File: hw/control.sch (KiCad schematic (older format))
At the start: 12 parts, among them U201 XTAL_OSC, U202 74HC74, U203 74HC161, U204 74HC574, U205 27C64, U206 27C64, U207 27C64, U208 27C64, U209 74HCT574, U210 74HCT574, U211 74HCT574, U212 74HCT574

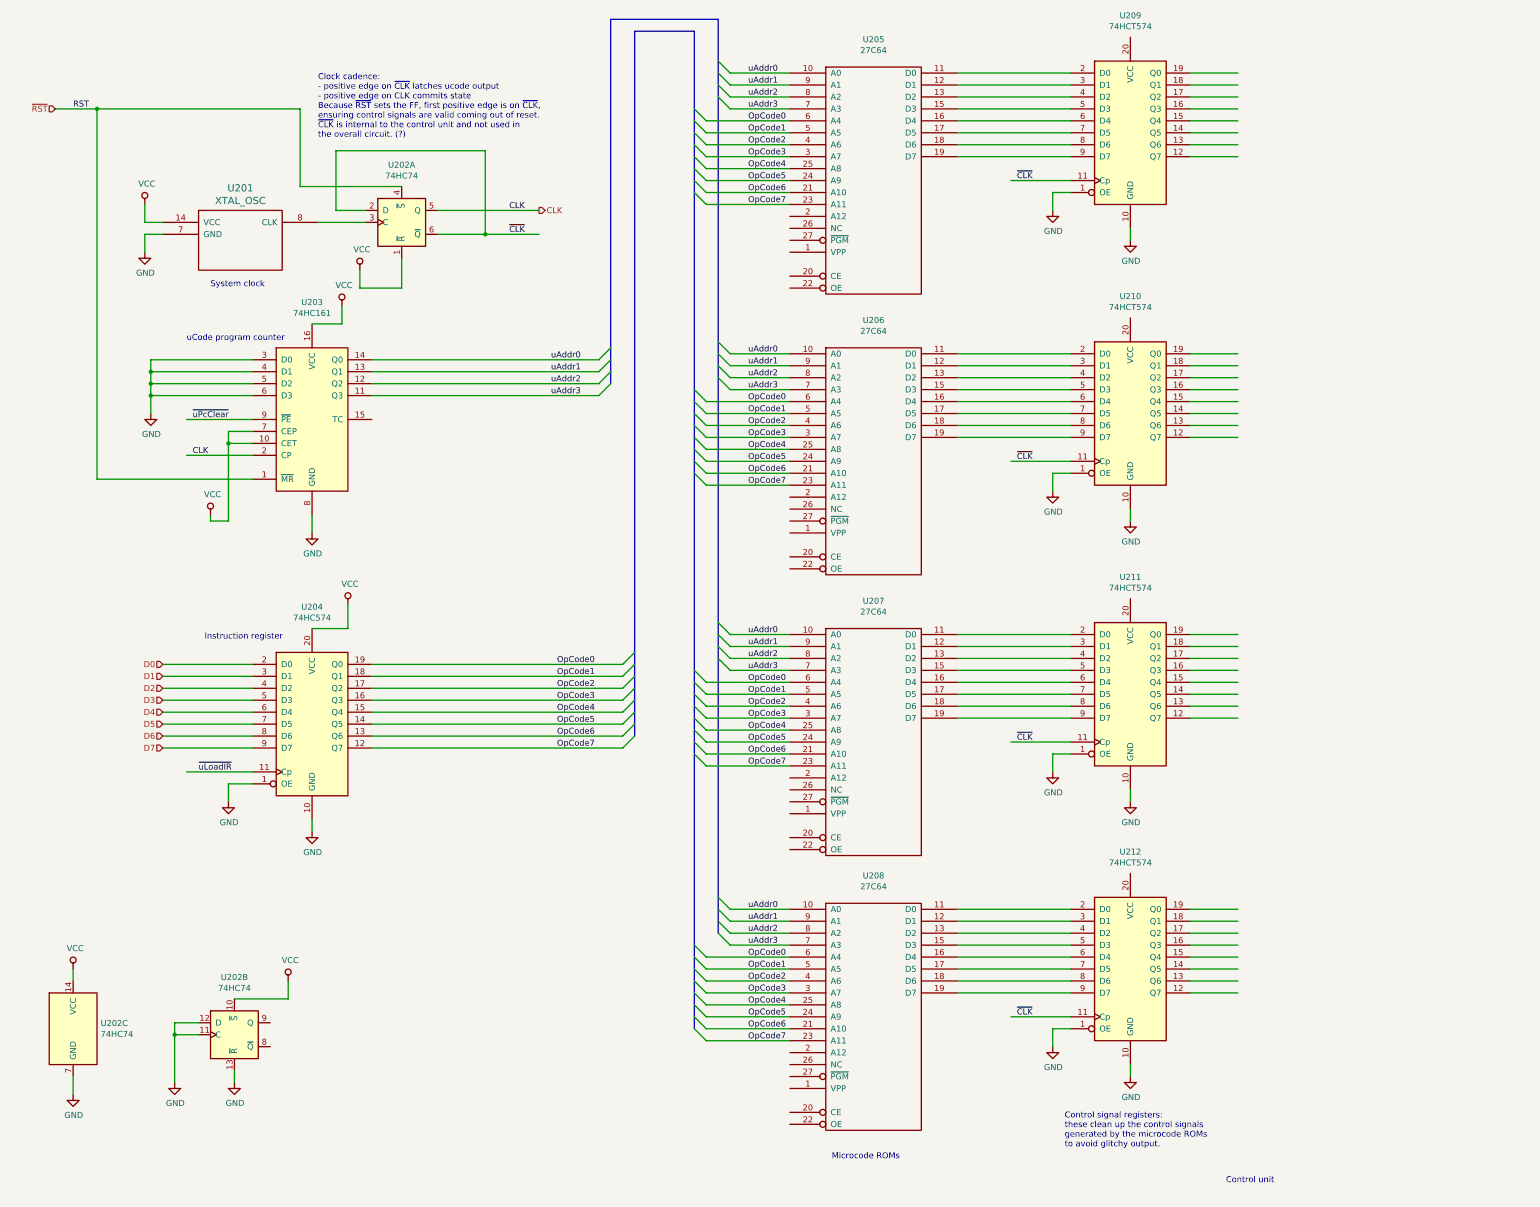
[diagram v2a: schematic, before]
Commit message: control cleanup, generate proper clock for IR load
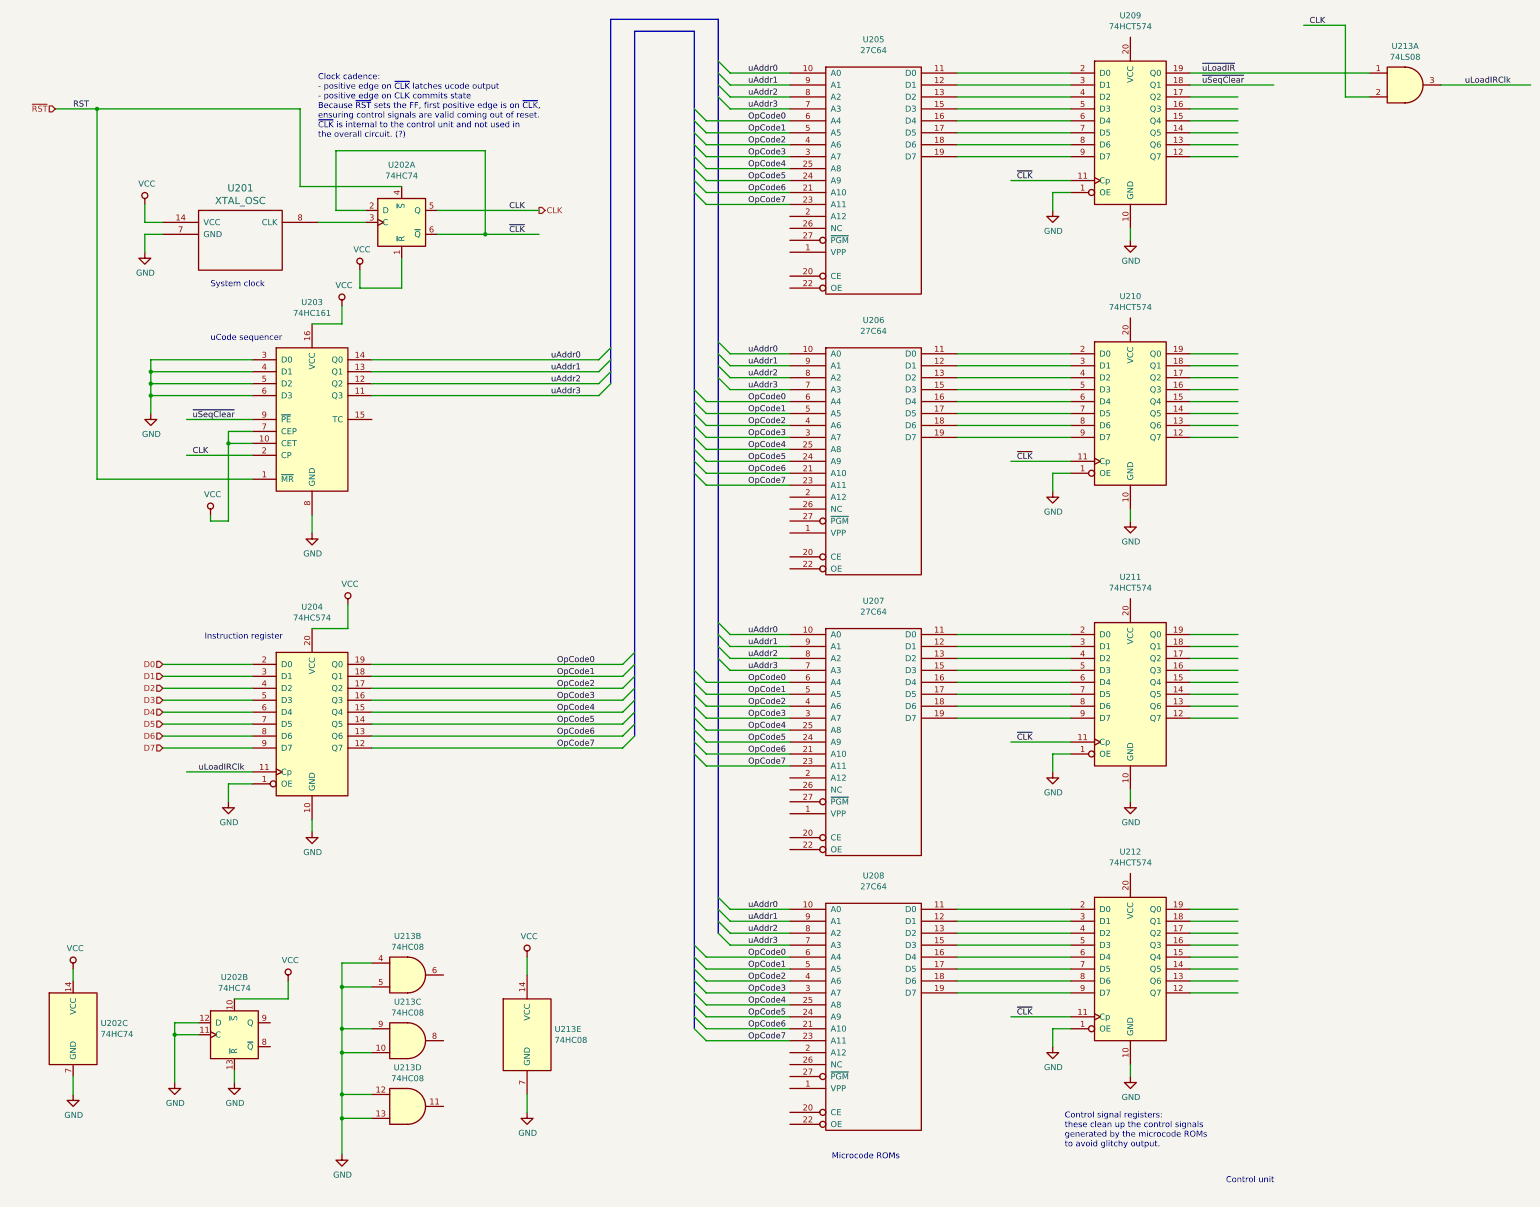
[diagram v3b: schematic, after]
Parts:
- added U213: 74LS08, symbol 74xx:74LS08
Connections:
- net labels added: uLoadIRClk, ~uSeqClear
- net labels removed: ~uPcClear
- wire segments 203 -> 221
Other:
- note added: "uCode sequencer"
- note removed: "uCode program counter"
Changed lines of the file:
@@
 	2650 3950 2100 3950
 Text Label 2150 3950 0    50   ~ 0
-~uPcClear
+~uSeqClear
 Wire Wire Line
 	2650 4250 2100 4250
@@
 	1    0    0    -1
 $EndComp
-Text Notes 2100 3300 0    50   ~ 0
-uCode program counter
+Text Notes 2300 3300 0    50   ~ 0
+uCode sequencer
 Text Label 5150 3450 0    50   ~ 0
 uAddr0
@@
 OpCode7
 Text Label 2200 6900 0    50   ~ 0
-~uLoadIR
+uLoadIRClk
 Wire Wire Line
 	3650 3450 5550 3450
@@
 $EndComp
 Wire Wire Line
-	10500 1050 10900 1050
-Wire Wire Line
-	10500 1150 10900 1150
-Wire Wire Line
 	10500 1250 10900 1250
 Wire Wire Line
@@
 Text Notes 9450 10050 0    50   ~ 0
 Control signal registers:\nthese clean up the control signals\ngenerated by the microcode ROMs\nto avoid glitchy output.
+$Comp
+L 74xx:74LS08 U213
+U 1 1 5DA375ED
+P 12300 1150
+F 0 "U213" H 12300 1475 50  0000 C CNN
+F 1 "74LS08" H 12300 1384 50  0000 C CNN
+F 2 "" H 12300 1150 50  0001 C CNN
+F 3 "" H 12300 1150 50  0001 C CNN
+	1    12300 1150
+	1    0    0    -1
+$EndComp
+Wire Wire Line
+	12000 1250 11800 1250
+Wire Wire Line
+	11800 1250 11800 650
+Wire Wire Line
+	11800 650  11450 650
+Text Label 11500 650  0    50   ~ 0
+CLK
+Wire Wire Line
+	10500 1050 12000 1050
+Text Label 10600 1050 0    50   ~ 0
+~uLoadIR
+Wire Wire Line
+	12600 1150 13350 1150
+Text Label 12800 1150 0    50   ~ 0
+uLoadIRClk
+Wire Wire Line
+	10500 1150 11200 1150
+Text Label 10600 1150 0    50   ~ 0
+~uSeqClear
+$Comp
+L 74xx:74LS08 U213
+U 2 1 5DA7CE65
+P 3950 8600
+F 0 "U213" H 3950 8925 50  0000 C CNN
+F 1 "74HC08" H 3950 8834 50  0000 C CNN
+F 2 "" H 3950 8600 50  0001 C CNN
+F 3 "" H 3950 8600 50  0001 C CNN
+	2    3950 8600
+	1    0    0    -1
+$EndComp
+$Comp
+L 74xx:74LS08 U213
+U 3 1 5DA7E038
+P 3950 9150
+F 0 "U213" H 3950 9475 50  0000 C CNN
+F 1 "74HC08" H 3950 9384 50  0000 C CNN
+F 2 "" H 3950 9150 50  0001 C CNN
+F 3 "" H 3950 9150 50  0001 C CNN
+	3    3950 9150
+	1    0    0    -1
+$EndComp
+$Comp
+L 74xx:74LS08 U213
+U 4 1 5DA82038
+P 3950 9700
+F 0 "U213" H 3950 10025 50  0000 C CNN
+F 1 "74HC08" H 3950 9934 50  0000 C CNN
+F 2 "" H 3950 9700 50  0001 C CNN
+F 3 "" H 3950 9700 50  0001 C CNN
+	4    3950 9700
+	1    0    0    -1
+$EndComp
+Wire Wire Line
+	3650 8500 3400 8500
+Wire Wire Line
+	3400 8500 3400 8700
+Wire Wire Line
+	3650 8700 3400 8700
+Connection ~ 3400 8700
+Wire Wire Line
+	3400 8700 3400 9050
+Wire Wire Line
+	3650 9050 3400 9050
+Connection ~ 3400 9050
+Wire Wire Line
+	3400 9050 3400 9250
+Wire Wire Line
+	3650 9250 3400 9250
+Connection ~ 3400 9250
+Wire Wire Line
+	3400 9250 3400 9600
+Wire Wire Line
+	3650 9600 3400 9600
+Connection ~ 3400 9600
+Wire Wire Line
+	3400 9600 3400 9800
+Wire Wire Line
+	3650 9800 3400 9800
+Connection ~ 3400 9800
+Wire Wire Line
+	3400 9800 3400 10100
+$Comp
+L 74xx:74LS08 U213
+U 5 1 5DAFA716
+P 4950 9100
+F 0 "U213" H 5180 9146 50  0000 L CNN
+F 1 "74HC08" H 5180 9055 50  0000 L CNN
+F 2 "" H 4950 9100 50  0001 C CNN
+F 3 "" H 4950 9100 50  0001 C CNN
+	5    4950 9100
+	1    0    0    -1
+$EndComp
+$Comp
+L power:GND #PWR?
+U 1 1 5DAFC25E
+P 3400 10100
+F 0 "#PWR?" H 3400 9850 50  0001 C CNN
+F 1 "GND" H 3405 9927 50  0000 C CNN
+F 2 "" H 3400 10100 50  0001 C CNN
+F 3 "" H 3400 10100 50  0001 C CNN
+	1    3400 10100
+	1    0    0    -1
+$EndComp
+Wire Wire Line
+	4950 8600 4950 8450
+Wire Wire Line
+	4950 9600 4950 9750
 Wire Bus Line
 	5650 600  5650 3650
@@
 Wire Bus Line
 	6350 700  6350 9050
+$Comp
+L power:VCC #PWR?
+U 1 1 5DB1ACB8
+P 4950 8450
+F 0 "#PWR?" H 4950 8300 50  0001 C CNN
+F 1 "VCC" H 4967 8623 50  0000 C CNN
+F 2 "" H 4950 8450 50  0001 C CNN
+F 3 "" H 4950 8450 50  0001 C CNN
+	1    4950 8450
+	1    0    0    -1
+$EndComp
+$Comp
+L power:GND #PWR?
+U 1 1 5DB1B425
+P 4950 9750
+F 0 "#PWR?" H 4950 9500 50  0001 C CNN
+F 1 "GND" H 4955 9577 50  0000 C CNN
+F 2 "" H 4950 9750 50  0001 C CNN
+F 3 "" H 4950 9750 50  0001 C CNN
+	1    4950 9750
+	1    0    0    -1
+$EndComp
 $EndSCHEMATC

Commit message: some cleanups/schematic improvements
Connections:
- wire segments 221 -> 265
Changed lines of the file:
@@
 EESchema Schematic File Version 4
 LIBS:easycpu-cache
-EELAYER 30 0
+EELAYER 26 0
 EELAYER END
 $Descr User 15400 11900
@@
 Wire Wire Line
 	4950 9600 4950 9750
+$Comp
+L power:VCC #PWR?
+U 1 1 5DB1ACB8
+P 4950 8450
+F 0 "#PWR?" H 4950 8300 50  0001 C CNN
+F 1 "VCC" H 4967 8623 50  0000 C CNN
+F 2 "" H 4950 8450 50  0001 C CNN
+F 3 "" H 4950 8450 50  0001 C CNN
+	1    4950 8450
+	1    0    0    -1
+$EndComp
+$Comp
+L power:GND #PWR?
+U 1 1 5DB1B425
+P 4950 9750
+F 0 "#PWR?" H 4950 9500 50  0001 C CNN
+F 1 "GND" H 4955 9577 50  0000 C CNN
+F 2 "" H 4950 9750 50  0001 C CNN
+F 3 "" H 4950 9750 50  0001 C CNN
+	1    4950 9750
+	1    0    0    -1
+$EndComp
+Wire Wire Line
+	7150 2250 6700 2250
+Wire Wire Line
+	6700 2250 6700 2750
+Wire Wire Line
+	7150 2750 6700 2750
+Connection ~ 6700 2750
+Wire Wire Line
+	6700 2750 6700 2850
+Wire Wire Line
+	7150 2850 6700 2850
+Connection ~ 6700 2850
+Wire Wire Line
+	6700 2850 6700 2950
+$Comp
+L power:GND #PWR?
+U 1 1 5DA86BF3
+P 6700 2950
+F 0 "#PWR?" H 6700 2700 50  0001 C CNN
+F 1 "GND" H 6705 2777 50  0000 C CNN
+F 2 "" H 6700 2950 50  0001 C CNN
+F 3 "" H 6700 2950 50  0001 C CNN
+	1    6700 2950
+	1    0    0    -1
+$EndComp
+Wire Wire Line
+	7150 2550 7000 2550
+Wire Wire Line
+	6800 2550 6800 2500
+$Comp
+L power:VCC #PWR?
+U 1 1 5DA966F2
+P 6800 2500
+F 0 "#PWR?" H 6800 2350 50  0001 C CNN
+F 1 "VCC" H 6817 2673 50  0000 C CNN
+F 2 "" H 6800 2500 50  0001 C CNN
+F 3 "" H 6800 2500 50  0001 C CNN
+	1    6800 2500
+	1    0    0    -1
+$EndComp
+Wire Wire Line
+	7150 2450 7000 2450
+Wire Wire Line
+	7000 2450 7000 2550
+Connection ~ 7000 2550
+Wire Wire Line
+	7000 2550 6800 2550
+Wire Wire Line
+	7150 4600 6700 4600
+Wire Wire Line
+	6700 4600 6700 5100
+Wire Wire Line
+	7150 5100 6700 5100
+Connection ~ 6700 5100
+Wire Wire Line
+	6700 5100 6700 5200
+Wire Wire Line
+	7150 5200 6700 5200
+Connection ~ 6700 5200
+Wire Wire Line
+	6700 5200 6700 5300
+$Comp
+L power:GND #PWR?
+U 1 1 5DAB60F4
+P 6700 5300
+F 0 "#PWR?" H 6700 5050 50  0001 C CNN
+F 1 "GND" H 6705 5127 50  0000 C CNN
+F 2 "" H 6700 5300 50  0001 C CNN
+F 3 "" H 6700 5300 50  0001 C CNN
+	1    6700 5300
+	1    0    0    -1
+$EndComp
+Wire Wire Line
+	7150 4900 7000 4900
+Wire Wire Line
+	6800 4900 6800 4850
+$Comp
+L power:VCC #PWR?
+U 1 1 5DAB60FC
+P 6800 4850
+F 0 "#PWR?" H 6800 4700 50  0001 C CNN
+F 1 "VCC" H 6817 5023 50  0000 C CNN
+F 2 "" H 6800 4850 50  0001 C CNN
+F 3 "" H 6800 4850 50  0001 C CNN
+	1    6800 4850
+	1    0    0    -1
+$EndComp
+Wire Wire Line
+	7150 4800 7000 4800
+Wire Wire Line
+	7000 4800 7000 4900
+Connection ~ 7000 4900
+Wire Wire Line
+	7000 4900 6800 4900
+Wire Wire Line
+	7150 6950 6700 6950
+Wire Wire Line
+	6700 6950 6700 7450
+Wire Wire Line
+	7150 7450 6700 7450
+Connection ~ 6700 7450
+Wire Wire Line
+	6700 7450 6700 7550
+Wire Wire Line
+	7150 7550 6700 7550
+Connection ~ 6700 7550
+Wire Wire Line
+	6700 7550 6700 7650
+$Comp
+L power:GND #PWR?
+U 1 1 5DAC810E
+P 6700 7650
+F 0 "#PWR?" H 6700 7400 50  0001 C CNN
+F 1 "GND" H 6705 7477 50  0000 C CNN
+F 2 "" H 6700 7650 50  0001 C CNN
+F 3 "" H 6700 7650 50  0001 C CNN
+	1    6700 7650
+	1    0    0    -1
+$EndComp
+Wire Wire Line
+	7150 7250 7000 7250
+Wire Wire Line
+	6800 7250 6800 7200
+$Comp
+L power:VCC #PWR?
+U 1 1 5DAC8116
+P 6800 7200
+F 0 "#PWR?" H 6800 7050 50  0001 C CNN
+F 1 "VCC" H 6817 7373 50  0000 C CNN
+F 2 "" H 6800 7200 50  0001 C CNN
+F 3 "" H 6800 7200 50  0001 C CNN
+	1    6800 7200
+	1    0    0    -1
+$EndComp
+Wire Wire Line
+	7150 7150 7000 7150
+Wire Wire Line
+	7000 7150 7000 7250
+Connection ~ 7000 7250
+Wire Wire Line
+	7000 7250 6800 7250
+Wire Wire Line
+	7150 9250 6700 9250
+Wire Wire Line
+	6700 9250 6700 9750
+Wire Wire Line
+	7150 9750 6700 9750
+Connection ~ 6700 9750
+Wire Wire Line
+	6700 9750 6700 9850
+Wire Wire Line
+	7150 9850 6700 9850
+Connection ~ 6700 9850
+Wire Wire Line
+	6700 9850 6700 9950
+$Comp
+L power:GND #PWR?
+U 1 1 5DADB612
+P 6700 9950
+F 0 "#PWR?" H 6700 9700 50  0001 C CNN
+F 1 "GND" H 6705 9777 50  0000 C CNN
+F 2 "" H 6700 9950 50  0001 C CNN
+F 3 "" H 6700 9950 50  0001 C CNN
+	1    6700 9950
+	1    0    0    -1
+$EndComp
+Wire Wire Line
+	7150 9550 7000 9550
+Wire Wire Line
+	6800 9550 6800 9500
+$Comp
+L power:VCC #PWR?
+U 1 1 5DADB61A
+P 6800 9500
+F 0 "#PWR?" H 6800 9350 50  0001 C CNN
+F 1 "VCC" H 6817 9673 50  0000 C CNN
+F 2 "" H 6800 9500 50  0001 C CNN
+F 3 "" H 6800 9500 50  0001 C CNN
+	1    6800 9500
+	1    0    0    -1
+$EndComp
+Wire Wire Line
+	7150 9450 7000 9450
+Wire Wire Line
+	7000 9450 7000 9550
+Connection ~ 7000 9550
+Wire Wire Line
+	7000 9550 6800 9550
 Wire Bus Line
 	5650 600  5650 3650
@@
 Wire Bus Line
 	6350 700  6350 9050
-$Comp
-L power:VCC #PWR?
-U 1 1 5DB1ACB8
-P 4950 8450
-F 0 "#PWR?" H 4950 8300 50  0001 C CNN
-F 1 "VCC" H 4967 8623 50  0000 C CNN
-F 2 "" H 4950 8450 50  0001 C CNN
-F 3 "" H 4950 8450 50  0001 C CNN
-	1    4950 8450
-	1    0    0    -1
-$EndComp
-$Comp
-L power:GND #PWR?
-U 1 1 5DB1B425
-P 4950 9750
-F 0 "#PWR?" H 4950 9500 50  0001 C CNN
-F 1 "GND" H 4955 9577 50  0000 C CNN
-F 2 "" H 4950 9750 50  0001 C CNN
-F 3 "" H 4950 9750 50  0001 C CNN
-	1    4950 9750
-	1    0    0    -1
-$EndComp
 $EndSCHEMATC
